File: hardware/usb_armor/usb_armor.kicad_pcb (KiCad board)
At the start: 2 copper layers, 29 x 29 mm, 20 parts, among them J1 USB, J2 USB

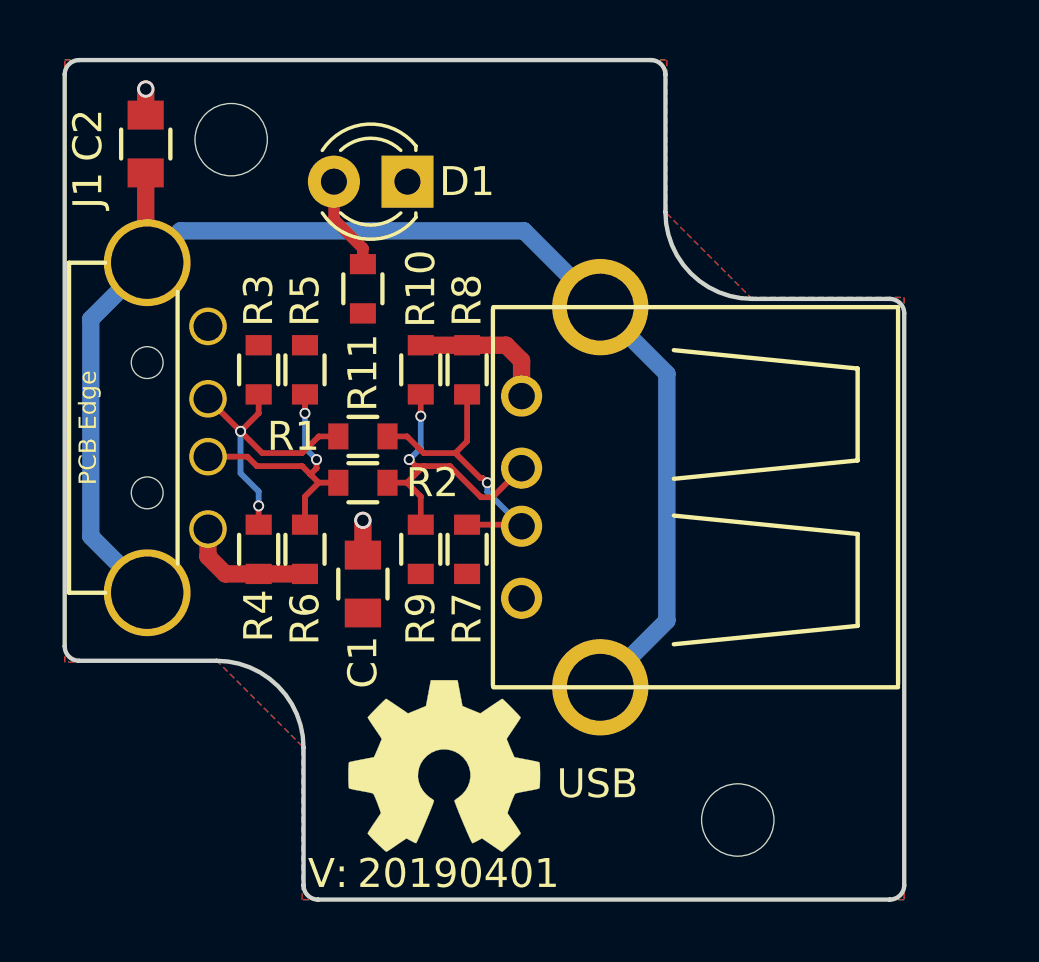
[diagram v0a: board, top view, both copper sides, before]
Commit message: modified board outline, WIP fixes
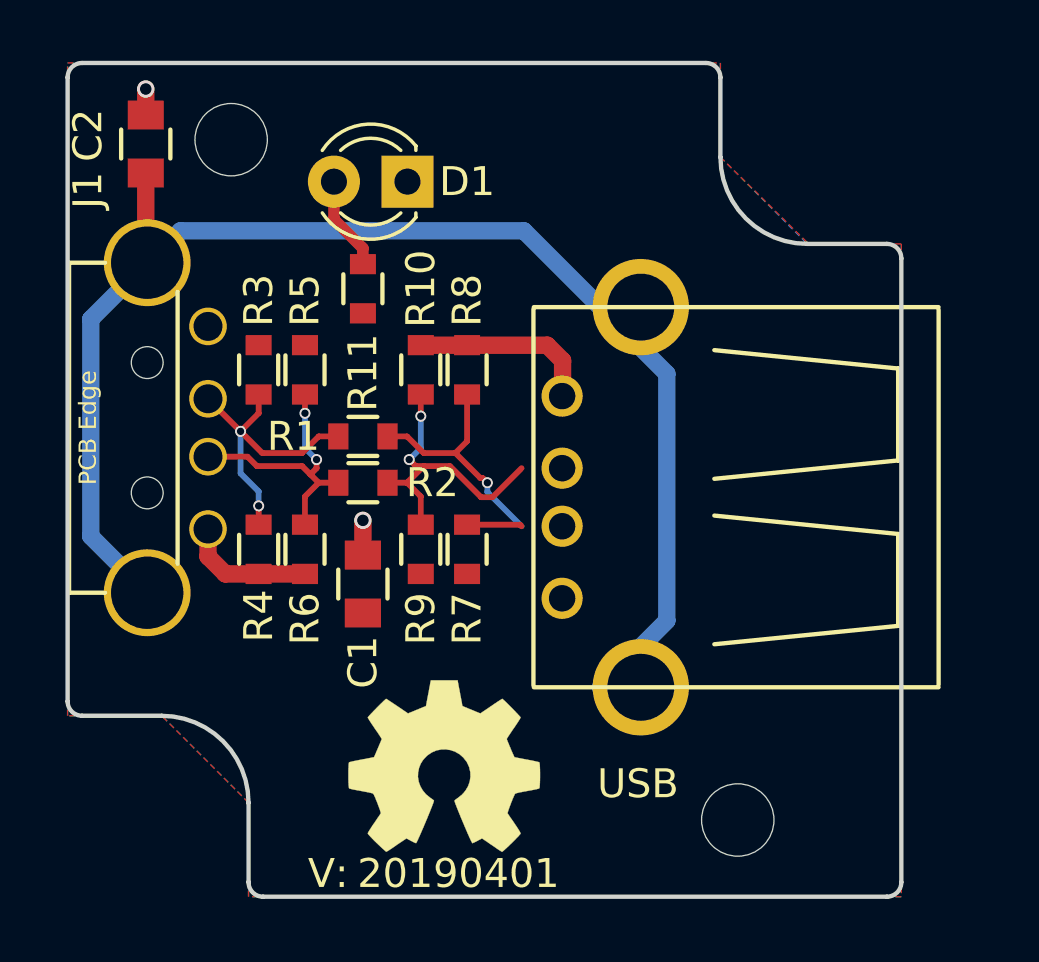
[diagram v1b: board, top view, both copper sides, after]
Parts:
- moved J2 1.40 mm to (153.3, 101.9)
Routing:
- net /GND: track 11.6 -> 13.0 mm
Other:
- board size 29 x 29 mm -> 28.8 x 28.8 mm
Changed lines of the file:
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@@
-(kicad_pcb (version 20171130) (host pcbnew 5.1.0-060a0da~80~ubuntu18.04.1)
+(kicad_pcb (version 20171130) (host pcbnew 5.1.2-f72e74a~84~ubuntu18.04.1)
   (general
     (thickness 1.6)
@@
   )
   (setup
-    (last_trace_width 0.4)
+    (last_trace_width 0.6)
     (user_trace_width 0.1524)
     (user_trace_width 0.2)
@@
   )
   (module SquantorUsb:USB-A-TH (layer F.Cu)
-    (at 151.9 101.9 180)
+    (at 153.3 101.9 180)
     (descr "USB SERIES A HOLE MOUNTED")
     (tags "USB SERIES A HOLE MOUNTED")
@@
     )
   )
-  (gr_arc (start 138.649999 110.55) (end 141.649999 110.55) (angle -89.9999809) (layer Edge.Cuts) (width 0.15))
-  (gr_arc (start 161.9 95.55) (end 162.4 95.55) (angle -90) (layer Edge.Cuts) (width 0.15))
-  (gr_arc (start 161.9 115.3) (end 161.9 115.8) (angle -90) (layer Edge.Cuts) (width 0.15))
-  (gr_arc (start 142.15 115.3) (end 141.65 115.3) (angle -90) (layer Edge.Cuts) (width 0.15))
-  (gr_arc (start 133.9 107.05) (end 133.4 107.05) (angle -90) (layer Edge.Cuts) (width 0.15))
-  (gr_arc (start 133.9 87.3) (end 133.9 86.8) (angle -90) (layer Edge.Cuts) (width 0.15))
-  (gr_line (start 133.4 107.05) (end 133.4 87.3) (layer Edge.Cuts) (width 0.15))
-  (gr_line (start 138.65 107.55) (end 133.9 107.55) (layer Edge.Cuts) (width 0.15))
-  (gr_line (start 141.65 115.3) (end 141.65 110.55) (layer Edge.Cuts) (width 0.15))
-  (gr_line (start 161.9 115.8) (end 142.15 115.8) (layer Edge.Cuts) (width 0.15))
-  (gr_line (start 162.4 95.55) (end 162.4 115.3) (layer Edge.Cuts) (width 0.15))
-  (gr_line (start 157.15 95.05) (end 161.9 95.05) (layer Edge.Cuts) (width 0.15))
-  (gr_arc (start 157.15 92.05) (end 154.15 92.05) (angle -89.9999809) (layer Edge.Cuts) (width 0.15))
-  (gr_line (start 154.15 87.3) (end 154.15 92.05) (layer Edge.Cuts) (width 0.15))
-  (gr_arc (start 153.65 87.3) (end 154.15 87.3) (angle -90) (layer Edge.Cuts) (width 0.15))
-  (gr_line (start 133.9 86.8) (end 153.65 86.8) (layer Edge.Cuts) (width 0.15))
+  (gr_arc (start 136.75 112.45) (end 139.75 112.45) (angle -89.9999809) (layer Edge.Cuts) (width 0.15))
+  (gr_arc (start 161.8 93.65) (end 162.3 93.65) (angle -90) (layer Edge.Cuts) (width 0.15))
+  (gr_arc (start 161.8 115.2) (end 161.8 115.7) (angle -90) (layer Edge.Cuts) (width 0.15))
+  (gr_arc (start 140.25 115.2) (end 139.75 115.2) (angle -90) (layer Edge.Cuts) (width 0.15))
+  (gr_arc (start 134 108.95) (end 133.5 108.95) (angle -90) (layer Edge.Cuts) (width 0.15))
+  (gr_arc (start 134 87.4) (end 134 86.9) (angle -90) (layer Edge.Cuts) (width 0.15))
+  (gr_line (start 133.5 108.95) (end 133.5 87.4) (layer Edge.Cuts) (width 0.15))
+  (gr_line (start 136.750001 109.45) (end 134 109.45) (layer Edge.Cuts) (width 0.15))
+  (gr_line (start 139.75 115.2) (end 139.75 112.45) (layer Edge.Cuts) (width 0.15))
+  (gr_line (start 161.8 115.7) (end 140.25 115.7) (layer Edge.Cuts) (width 0.15))
+  (gr_line (start 162.3 93.65) (end 162.3 115.2) (layer Edge.Cuts) (width 0.15))
+  (gr_line (start 159.049999 93.15) (end 161.8 93.15) (layer Edge.Cuts) (width 0.15))
+  (gr_arc (start 159.05 90.15) (end 156.05 90.15) (angle -89.9999809) (layer Edge.Cuts) (width 0.15))
+  (gr_line (start 156.05 87.4) (end 156.05 90.15) (layer Edge.Cuts) (width 0.15))
+  (gr_arc (start 155.55 87.4) (end 156.05 87.4) (angle -90) (layer Edge.Cuts) (width 0.15))
+  (gr_line (start 134 86.9) (end 155.55 86.9) (layer Edge.Cuts) (width 0.15))
   (segment (start 141.7 104.55) (end 140.1 104.55) (width 0.6) (layer F.Cu) (net 2))
   (segment (start 140.1 104.55) (end 138.95 104.55) (width 0.6) (layer F.Cu) (net 2))
@@
   (segment (start 138.95 104.55) (end 138.35 103.95) (width 0.6) (layer F.Cu) (net 2))
   (segment (start 145.7 96.65) (end 147.3 96.65) (width 0.6) (layer F.Cu) (net 2))
-  (segment (start 147.3 96.65) (end 148.65 96.65) (width 0.6) (layer F.Cu) (net 2))
-  (segment (start 149.1822 97.1822) (end 149.1822 98.4075) (width 0.6) (layer F.Cu) (net 2))
-  (segment (start 148.65 96.65) (end 149.1822 97.1822) (width 0.6) (layer F.Cu) (net 2))
   (via (at 136.2 87.8) (size 0.6) (drill 0.4) (layers F.Cu B.Cu) (net 2))
   (segment (start 136.2 88.7) (end 136.2 87.8) (width 0.6) (layer F.Cu) (net 2))
   (via (at 143.7 102.7) (size 0.6) (drill 0.4) (layers F.Cu B.Cu) (net 2))
   (segment (start 143.7 103.9) (end 143.7 102.7) (width 0.6) (layer F.Cu) (net 2))
+  (segment (start 150.6 97.1822) (end 150.6 98.4075) (width 0.6) (layer F.Cu) (net 2))
+  (segment (start 147.3 96.65) (end 150.0678 96.65) (width 0.6) (layer F.Cu) (net 2))
+  (segment (start 150.0678 96.65) (end 150.6 97.1822) (width 0.6) (layer F.Cu) (net 2))
   (segment (start 151.9 95.3341) (end 154.2 97.6341) (width 0.6) (layer B.Cu) (net 3))
   (segment (start 154.2 106.1659) (end 151.9 108.4659) (width 0.6) (layer B.Cu) (net 3))
@@
     (polygon
       (pts
-        (xy 133.4 86.8) (xy 154.2 86.8) (xy 154.2 92.1) (xy 157.1 95) (xy 162.4 95)
-        (xy 162.4 115.8) (xy 141.6 115.8) (xy 141.6 110.5) (xy 138.7 107.6) (xy 133.4 107.6)
+        (xy 133.5 86.9) (xy 156.05 86.9) (xy 156.05 90.15) (xy 159.05 93.15) (xy 162.3 93.15)
+        (xy 162.3 115.7) (xy 139.75 115.7) (xy 139.75 112.45) (xy 136.75 109.45) (xy 133.5 109.45)
       )
     )
@@
     (polygon
       (pts
-        (xy 133.4 86.8) (xy 154.2 86.8) (xy 154.2 92.1) (xy 157.1 95) (xy 162.4 95)
-        (xy 162.4 115.8) (xy 141.6 115.8) (xy 141.6 110.5) (xy 138.7 107.6) (xy 133.4 107.6)
+        (xy 133.5 86.9) (xy 156.05 86.9) (xy 156.05 90.15) (xy 159.1 93.15) (xy 162.3 93.15)
+        (xy 162.3 115.7) (xy 139.75 115.7) (xy 139.75 112.45) (xy 136.75 109.45) (xy 133.5 109.45)
       )
     )

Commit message: fixed incorrect input connector
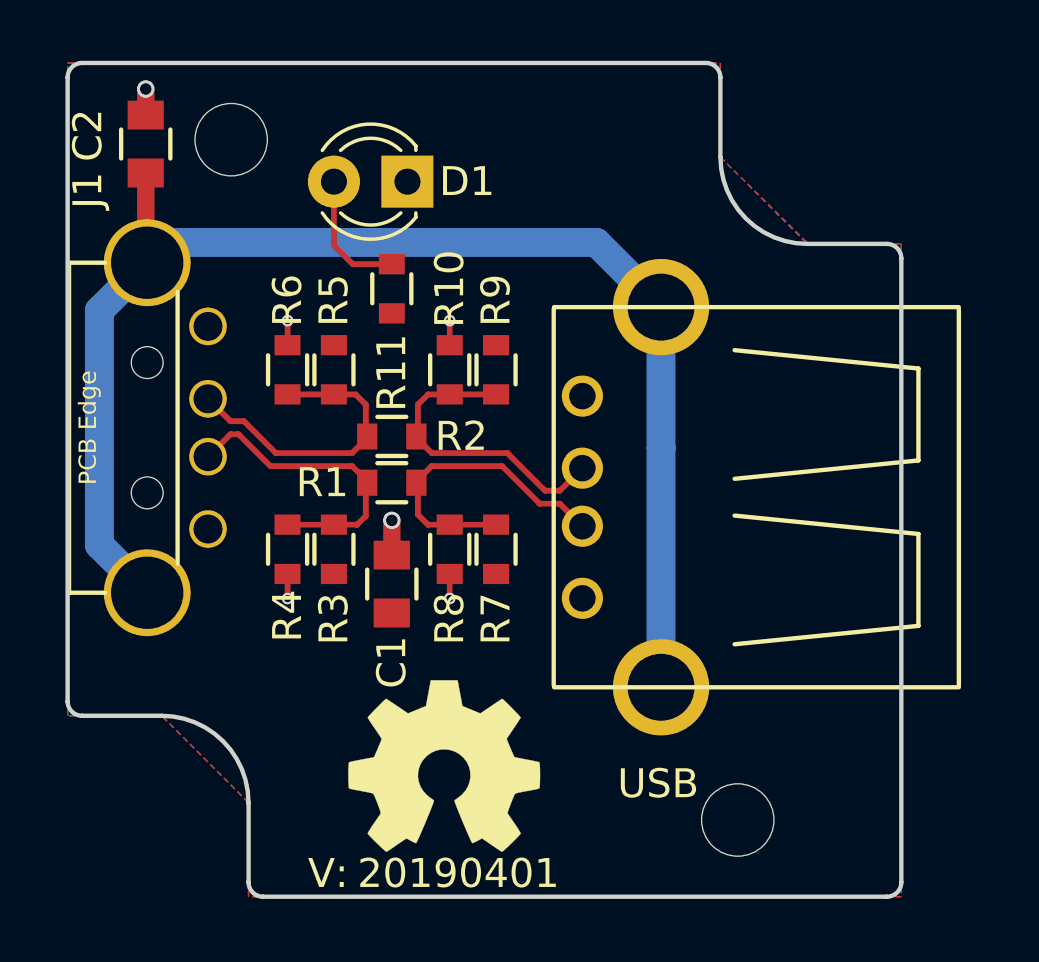
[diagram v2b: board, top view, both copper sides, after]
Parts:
- moved R9 6.72 mm to (148.3, 97.5), turned to 90 degrees
- moved R3 6.72 mm to (142.7, 103.7), turned to 270 degrees
- moved R8 6.23 mm to (146.7, 103.7), turned to 90 degrees
- moved R6 6.23 mm to (141.1, 97.5), turned to 270 degrees
- moved R1 1.89 mm to (144.7, 101.4)
- moved R2 1.89 mm to (144.7, 99.8)
- moved C1 1.00 mm to (144.7, 104.9)
- moved R10 1.00 mm to (146.7, 97.5)
- moved R11 1.00 mm to (144.7, 94.7)
- moved R4 1.00 mm to (141.1, 103.7)
- moved R5 1.00 mm to (142.7, 97.5)
- moved R7 1.00 mm to (148.3, 103.7)
- moved J2 0.70 mm to (154.0, 101.9)
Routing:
- net /GND: track 13.0 -> 5.50 mm, vias 2 -> 6
- net Net-(D1-Pad2): track 3.26 -> 4.47 mm
- net /IN_USB-D+: track 9.54 -> 10.5 mm, vias 2 -> 0
- net /OUT_USB-D-: track 10.2 -> 10.8 mm, vias 1 -> 0
- net /OUT_USB-D+: track 10.4 -> 10.8 mm, vias 2 -> 0
- net /IN_USB-D-: vias 2 -> 0

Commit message: updated versionnumber
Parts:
- N2: value 20190401 -> 20190709
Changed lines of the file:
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@@
       (effects (font (size 1 1) (thickness 0.15)))
     )
-    (fp_text value 20190401 (at -0.4 -0.1) (layer F.SilkS)
+    (fp_text value 20190709 (at -0.4 -0.1) (layer F.SilkS)
       (effects (font (size 1 1) (thickness 0.15)))
     )

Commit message: shifted usb connector more outside
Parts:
- moved J2 0.70 mm to (154.7, 101.9)
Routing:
- net /OUT_USB-D+: track 10.8 -> 11.5 mm
- net /OUT_USB-D-: track 10.8 -> 11.5 mm
- net /Shield: track 48.0 -> 48.7 mm
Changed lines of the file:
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@@
     (thickness 1.6)
     (drawings 16)
-    (tracks 64)
+    (tracks 65)
     (zones 0)
     (modules 20)
@@
   )
   (setup
-    (last_trace_width 0.2)
+    (last_trace_width 1)
     (user_trace_width 0.1524)
     (user_trace_width 0.2)
@@
   )
   (module SquantorUsb:USB-A-TH (layer F.Cu)
-    (at 154 101.9 180)
+    (at 154.7 101.9 180)
     (descr "USB SERIES A HOLE MOUNTED")
     (tags "USB SERIES A HOLE MOUNTED")
@@
   (segment (start 134.6 95.45) (end 134.6 103.55) (width 1) (layer B.Cu) (net 3))
   (segment (start 136.95 93.1) (end 136.25 93.8) (width 1) (layer B.Cu) (net 3))
-  (segment (start 154 95.3341) (end 151.7659 93.1) (width 1) (layer B.Cu) (net 3))
   (segment (start 151.7659 93.1) (end 136.95 93.1) (width 1) (layer B.Cu) (net 3))
-  (segment (start 154 108.4659) (end 154 100.2) (width 1) (layer B.Cu) (net 3))
-  (segment (start 154 95.3341) (end 154 100.2) (width 1) (layer B.Cu) (net 3))
+  (segment (start 154.7 108.4659) (end 154.7 100.2) (width 1) (layer B.Cu) (net 3))
+  (segment (start 154.7 95.3341) (end 154.7 100.2) (width 1) (layer B.Cu) (net 3))
+  (segment (start 151.7659 93.1) (end 152.5 93.1) (width 1) (layer B.Cu) (net 3))
+  (segment (start 152.5 93.1) (end 154.7 95.3) (width 1) (layer B.Cu) (net 3))
   (segment (start 139.125 99.725) (end 138.35 100.5) (width 0.2) (layer F.Cu) (net 4))
   (segment (start 139.4068 99.725) (end 139.125 99.725) (width 0.2) (layer F.Cu) (net 4))
@@
   (segment (start 141.1 98.35) (end 143.45 98.35) (width 0.2) (layer F.Cu) (net 5))
   (segment (start 143.45 98.35) (end 143.8 98.7) (width 0.2) (layer F.Cu) (net 5))
-  (segment (start 150.5039 101.675) (end 151.2822 100.8967) (width 0.2) (layer F.Cu) (net 6))
-  (segment (start 149.9932 101.675) (end 150.5039 101.675) (width 0.2) (layer F.Cu) (net 6))
   (segment (start 145.6 99.8) (end 145.7 99.9) (width 0.2) (layer F.Cu) (net 6))
   (segment (start 148.6932 100.375) (end 149.9932 101.675) (width 0.2) (layer F.Cu) (net 6))
@@
   (segment (start 145.95 98.35) (end 145.6 98.7) (width 0.2) (layer F.Cu) (net 6))
   (segment (start 145.6 98.7) (end 145.6 99.8) (width 0.2) (layer F.Cu) (net 6))
-  (segment (start 150.5039 102.125) (end 151.2822 102.9033) (width 0.2) (layer F.Cu) (net 7))
-  (segment (start 149.8068 102.125) (end 150.5039 102.125) (width 0.2) (layer F.Cu) (net 7))
+  (segment (start 151.2039 101.675) (end 151.9822 100.8967) (width 0.2) (layer F.Cu) (net 6))
+  (segment (start 149.9932 101.675) (end 151.2 101.675) (width 0.2) (layer F.Cu) (net 6))
   (segment (start 148.5068 100.825) (end 149.8068 102.125) (width 0.2) (layer F.Cu) (net 7))
   (segment (start 146.075 100.825) (end 148.5068 100.825) (width 0.2) (layer F.Cu) (net 7))
@@
   (segment (start 145.95 102.85) (end 145.6 102.5) (width 0.2) (layer F.Cu) (net 7))
   (segment (start 145.6 102.5) (end 145.6 101.4) (width 0.2) (layer F.Cu) (net 7))
+  (segment (start 151.2039 102.125) (end 151.9822 102.9033) (width 0.2) (layer F.Cu) (net 7))
+  (segment (start 149.8068 102.125) (end 151.2 102.125) (width 0.2) (layer F.Cu) (net 7))
   (segment (start 144.7 93.85) (end 143.35 93.85) (width 0.2) (layer F.Cu) (net 8))
   (segment (start 143.35 93.85) (end 142.7 93.2) (width 0.2) (layer F.Cu) (net 8))
